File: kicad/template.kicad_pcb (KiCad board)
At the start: 2 copper layers, 84.1 x 61.7 mm, 7 parts, among them J1 Bus_PCI_Express_x1, J6 USB_C_Receptacle_USB2.0_16P, U1 MCP25625T-E/ML, U2 RP2040, U4 W25Q128JVP, X1 ABM8-272-T3, Y1 X322516MLB4SI

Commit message: init cihad's status module
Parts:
- removed U1: MCP25625T-E/ML, challenge_template:QFN28_6X6MC_MCH
- removed Y1: X322516MLB4SI, challenge_template:OSC_X322516MLB4SI
- added S1: TS-1187A-B-A-B, TS-1187A-B-A-B:SW_TS-1187A-B-A-B, F.Cu at (162.0, 117.6)
- added S2: TS-1187A-B-A-B, TS-1187A-B-A-B:SW_TS-1187A-B-A-B, F.Cu at (130.9, 117.6)
- added U9: MCP25625T-E/ML, MCP25625T_E_ML:QFN28_6X6MC_MCH, F.Cu at (138.9, 87.6)
- X1: footprint challenge_template:ABM8-272-T3_ABR -> ABM8-272-T3:ABM8-272-T3_ABR
- moved X1 14.6 mm to (149.0, 88.0)
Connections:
- U4 pad 4: unconnected-(U4-GND-Pad4) -> GND
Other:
- board text added: "Boot"
- board text added: "Reset"

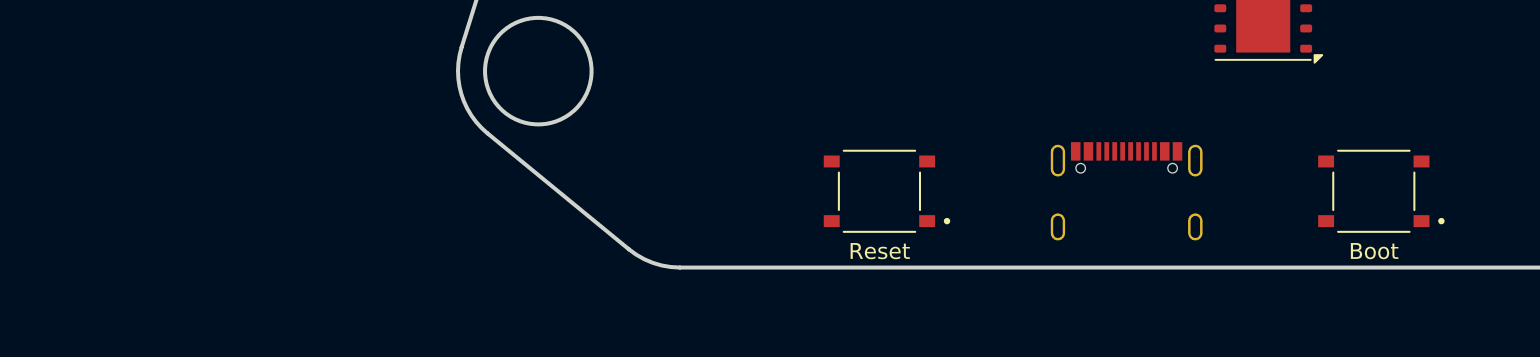
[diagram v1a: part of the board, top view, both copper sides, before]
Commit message: delete unessesary button
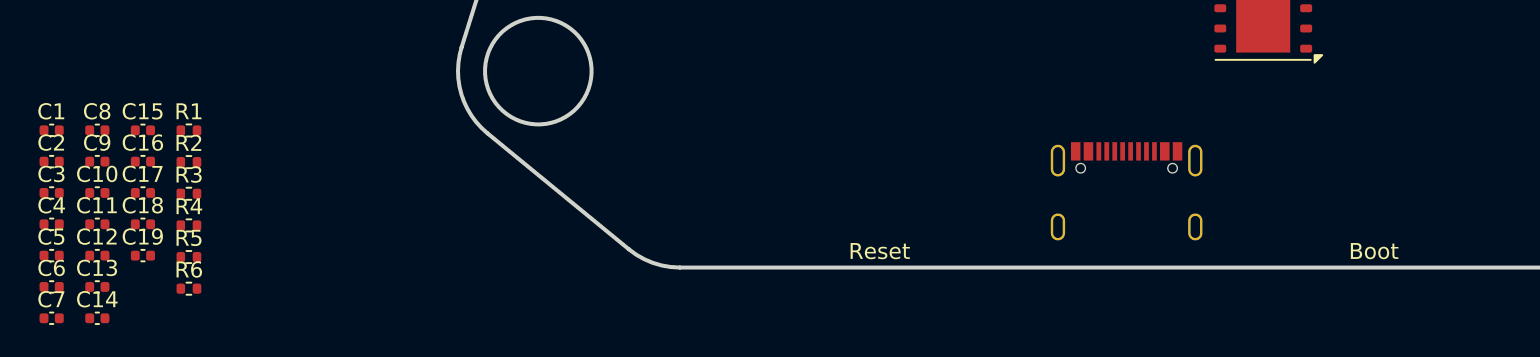
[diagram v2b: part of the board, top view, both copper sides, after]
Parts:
- removed S1, S2: TS-1187A-B-A-B, TS-1187A-B-A-B:SW_TS-1187A-B-A-B
- added C1: 100n, Capacitor_SMD:C_0402_1005Metric, F.Cu at (78.8, 113.8)
- added C10: 100n, Capacitor_SMD:C_0402_1005Metric, F.Cu at (81.7, 117.7)
- added C11: 100n, Capacitor_SMD:C_0402_1005Metric, F.Cu at (81.7, 119.7)
- added C12: 22p, Capacitor_SMD:C_0402_1005Metric, F.Cu at (81.7, 121.7)
- added C13: 22p, Capacitor_SMD:C_0402_1005Metric, F.Cu at (81.7, 123.6)
- added C14: 15p, Capacitor_SMD:C_0402_1005Metric, F.Cu at (81.7, 125.6)
- added C15: 15p, Capacitor_SMD:C_0402_1005Metric, F.Cu at (84.5, 113.8)
- added C16: 100n, Capacitor_SMD:C_0402_1005Metric, F.Cu at (84.5, 115.8)
- added C17: 100n, Capacitor_SMD:C_0402_1005Metric, F.Cu at (84.5, 117.7)
- added C18: 100n, Capacitor_SMD:C_0402_1005Metric, F.Cu at (84.5, 119.7)
- added C19: 100n, Capacitor_SMD:C_0402_1005Metric, F.Cu at (84.5, 121.7)
- added C2: 100n, Capacitor_SMD:C_0402_1005Metric, F.Cu at (78.8, 115.8)
- added C3: 1u, Capacitor_SMD:C_0402_1005Metric, F.Cu at (78.8, 117.7)
- added C4: 100n, Capacitor_SMD:C_0402_1005Metric, F.Cu at (78.8, 119.7)
- added C5: 1u, Capacitor_SMD:C_0402_1005Metric, F.Cu at (78.8, 121.7)
- added C6: 100n, Capacitor_SMD:C_0402_1005Metric, F.Cu at (78.8, 123.6)
- added C7: 100n, Capacitor_SMD:C_0402_1005Metric, F.Cu at (78.8, 125.6)
- added C8: 100n, Capacitor_SMD:C_0402_1005Metric, F.Cu at (81.7, 113.8)
- added C9: 100n, Capacitor_SMD:C_0402_1005Metric, F.Cu at (81.7, 115.8)
- added R1: 27, Resistor_SMD:R_0402_1005Metric, F.Cu at (87.4, 113.8)
- added R2: 27, Resistor_SMD:R_0402_1005Metric, F.Cu at (87.4, 115.8)
- added R3: 5.1k, Resistor_SMD:R_0402_1005Metric, F.Cu at (87.4, 117.8)
- added R4: 5.1k, Resistor_SMD:R_0402_1005Metric, F.Cu at (87.4, 119.8)
- added R5: 1k, Resistor_SMD:R_0402_1005Metric, F.Cu at (87.4, 121.8)
- added R6: 1k, Resistor_SMD:R_0402_1005Metric, F.Cu at (87.4, 123.8)
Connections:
- net Net-(J6-D+-PadA6) renamed USB_D+
- net Net-(J6-D--PadA7) renamed USB_D-
- J6 pad A5: unconnected-(J6-CC1-PadA5) -> Net-(J6-CC1)
- J6 pad B5: unconnected-(J6-CC2-PadB5) -> Net-(J6-CC2)
- U2 pad 1: Net-(U2-IOVDD-Pad1) -> +3V3
- U2 pad 10: Net-(U2-IOVDD-Pad1) -> +3V3
- U2 pad 19: unconnected-(U2-TESTEN-Pad19) -> GND
- U2 pad 20: unconnected-(U2-XIN-Pad20) -> /XIN
- U2 pad 21: unconnected-(U2-XOUT-Pad21) -> /XOUT
- U2 pad 22: Net-(U2-IOVDD-Pad1) -> +3V3
- U2 pad 23: Net-(U2-DVDD-Pad23) -> +1V1
- U2 pad 24: unconnected-(U2-SWCLK-Pad24) -> /SWCLK
- U2 pad 25: unconnected-(U2-SWD-Pad25) -> /SWD
- U2 pad 33: Net-(U2-IOVDD-Pad1) -> +3V3
- U2 pad 39: unconnected-(U2-GPIO27_ADC1-Pad39) -> INT
- U2 pad 40: unconnected-(U2-GPIO28_ADC2-Pad40) -> SDA
- U2 pad 41: unconnected-(U2-GPIO29_ADC3-Pad41) -> SCL
- U2 pad 42: Net-(U2-IOVDD-Pad1) -> +3V3
- U2 pad 43: unconnected-(U2-ADC_AVDD-Pad43) -> +3V3
- U2 pad 44: unconnected-(U2-VREG_IN-Pad44) -> +3V3
- U2 pad 45: unconnected-(U2-VREG_VOUT-Pad45) -> +1V1
- U2 pad 46: unconnected-(U2-USB_DM-Pad46) -> /USB_D2-
- U2 pad 47: unconnected-(U2-USB_DP-Pad47) -> /USB_D2+
- U2 pad 48: unconnected-(U2-USB_VDD-Pad48) -> +3V3
- U2 pad 49: Net-(U2-IOVDD-Pad1) -> +3V3
- U2 pad 50: Net-(U2-DVDD-Pad23) -> +1V1
- U2 pad 51: unconnected-(U2-QSPI_SD3-Pad51) -> /QSPI_SD3
- U2 pad 52: unconnected-(U2-QSPI_SCLK-Pad52) -> /QSPI_SCLK
- U2 pad 53: unconnected-(U2-QSPI_SD0-Pad53) -> /QSPI_SD0
- U2 pad 54: unconnected-(U2-QSPI_SD2-Pad54) -> /QSPI_SD2
- U2 pad 55: unconnected-(U2-QSPI_SD1-Pad55) -> /QSPI_SD1
- U2 pad 56: unconnected-(U2-QSPI_SS-Pad56) -> /QSPI_SS
- U2 pad 57: unconnected-(U2-GND-Pad57) -> GND
- U4 pad 1: unconnected-(U4-~{CS}-Pad1) -> /QSPI_SS
- U4 pad 2: unconnected-(U4-DO(IO1)-Pad2) -> /QSPI_SD1
- U4 pad 3: unconnected-(U4-IO2-Pad3) -> /QSPI_SD2
- U4 pad 4: GND -> unconnected-(U4-GND-Pad4)
- U4 pad 5: unconnected-(U4-DI(IO0)-Pad5) -> /QSPI_SD0
- U4 pad 6: unconnected-(U4-CLK-Pad6) -> /QSPI_SCLK
- U4 pad 7: unconnected-(U4-IO3-Pad7) -> /QSPI_SD3
- U4 pad 8: unconnected-(U4-VCC-Pad8) -> +3.3V
- U9 pad 10: unconnected-(U9-RXD-Pad10) -> rx(CAN)
- U9 pad 11: unconnected-(U9-VIO-Pad11) -> +3V3
- U9 pad 16: unconnected-(U9-TXD-Pad16) -> tx(CAN)
- U9 pad 19: unconnected-(U9-VDDA-Pad19) -> +5V
- U9 pad 20: unconnected-(U9-OSC2-Pad20) -> OSC2
- U9 pad 21: unconnected-(U9-OSC1-Pad21) -> OSC1
- U9 pad 3: unconnected-(U9-VDD-Pad3) -> +3V3
- U9 pad 4: unconnected-(U9-TXCAN-Pad4) -> tx(CAN)
- U9 pad 5: unconnected-(U9-RXCAN-Pad5) -> rx(CAN)
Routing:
- added copper zone on F.Cu, net +1V1
- removed copper zone on F.Cu, net unconnected-(U2-VREG_VOUT-Pad45)
